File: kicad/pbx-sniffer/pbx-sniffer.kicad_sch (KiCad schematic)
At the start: 6 parts, among them U1 STM32H7R3V8Tx, U4 MX25L3233FM2

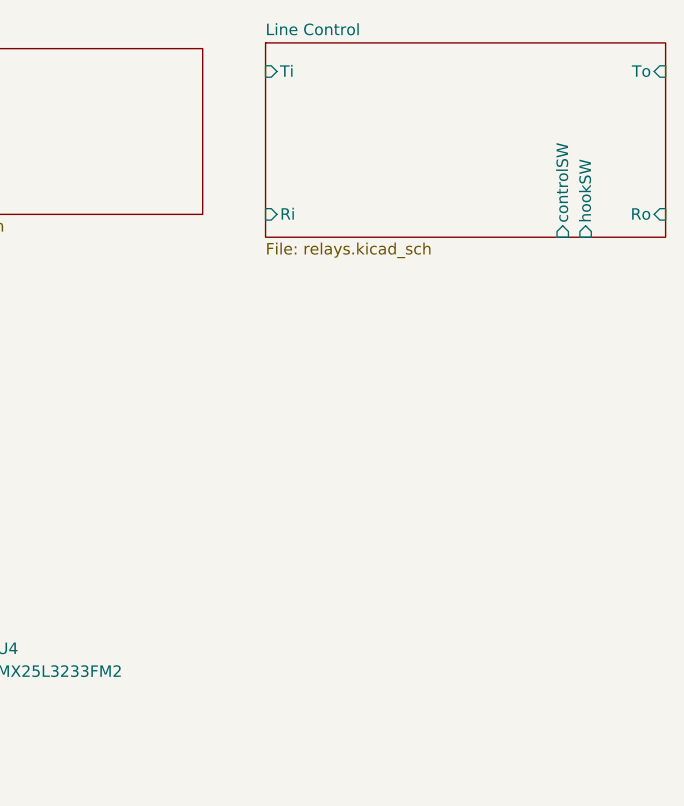
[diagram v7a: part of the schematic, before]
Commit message: added multiplexer and updated relay notation
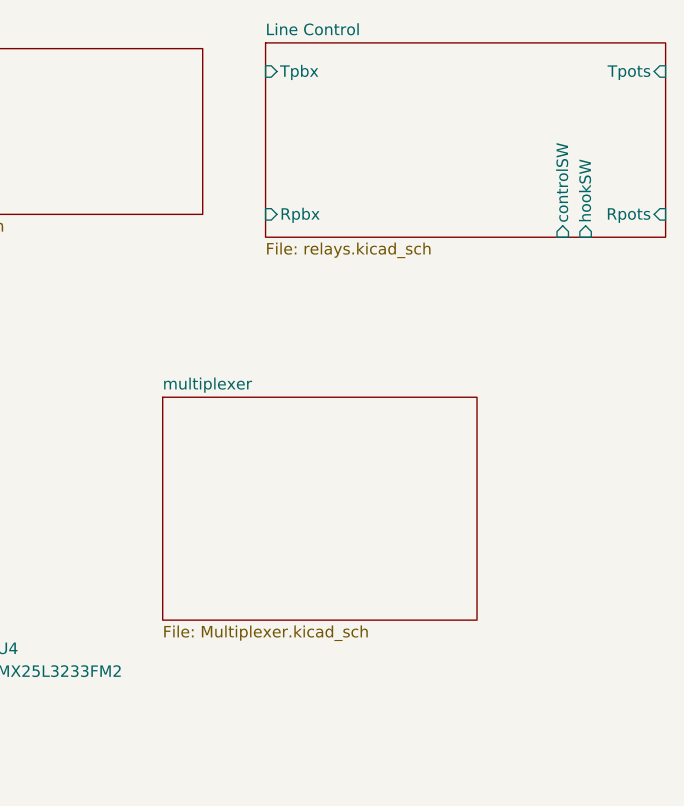
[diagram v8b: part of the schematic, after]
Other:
- added sheet multiplexer (Multiplexer.kicad_sch)
- sheet Line Control ports: added Rpbx, Rpots, Tpbx, Tpots; removed Ri, Ro, Ti, To
